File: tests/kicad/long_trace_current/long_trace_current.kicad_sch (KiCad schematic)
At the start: 2 parts

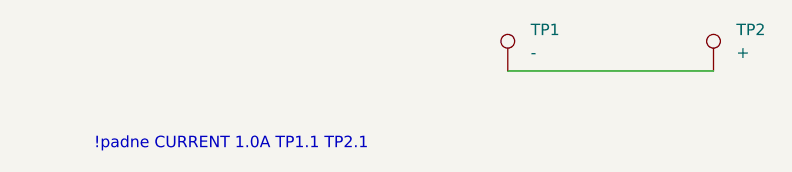
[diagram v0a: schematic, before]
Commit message: feat: Richer directive syntax
This commit adds support for named directive parameters. No more
guessing which parameter is the positive terminal positive and which is the
negative terminal!
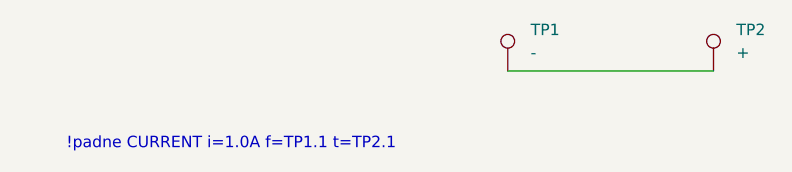
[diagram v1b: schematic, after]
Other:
- note added: "!padne CURRENT i=1.0A f=TP1.1 t=TP2.1"
- note removed: "!padne CURRENT 1.0A TP1.1 TP2.1"
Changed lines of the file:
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@@
 		)
 	)
-	(text "!padne CURRENT 1.0A TP1.1 TP2.1"
+	(text "!padne CURRENT i=1.0A f=TP1.1 t=TP2.1"
 		(exclude_from_sim no)
 		(at 79.756 107.188 0)
